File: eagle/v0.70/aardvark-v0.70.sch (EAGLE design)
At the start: 22 parts, among them IC1 REG1117, X1 MINI-USB-32005-201

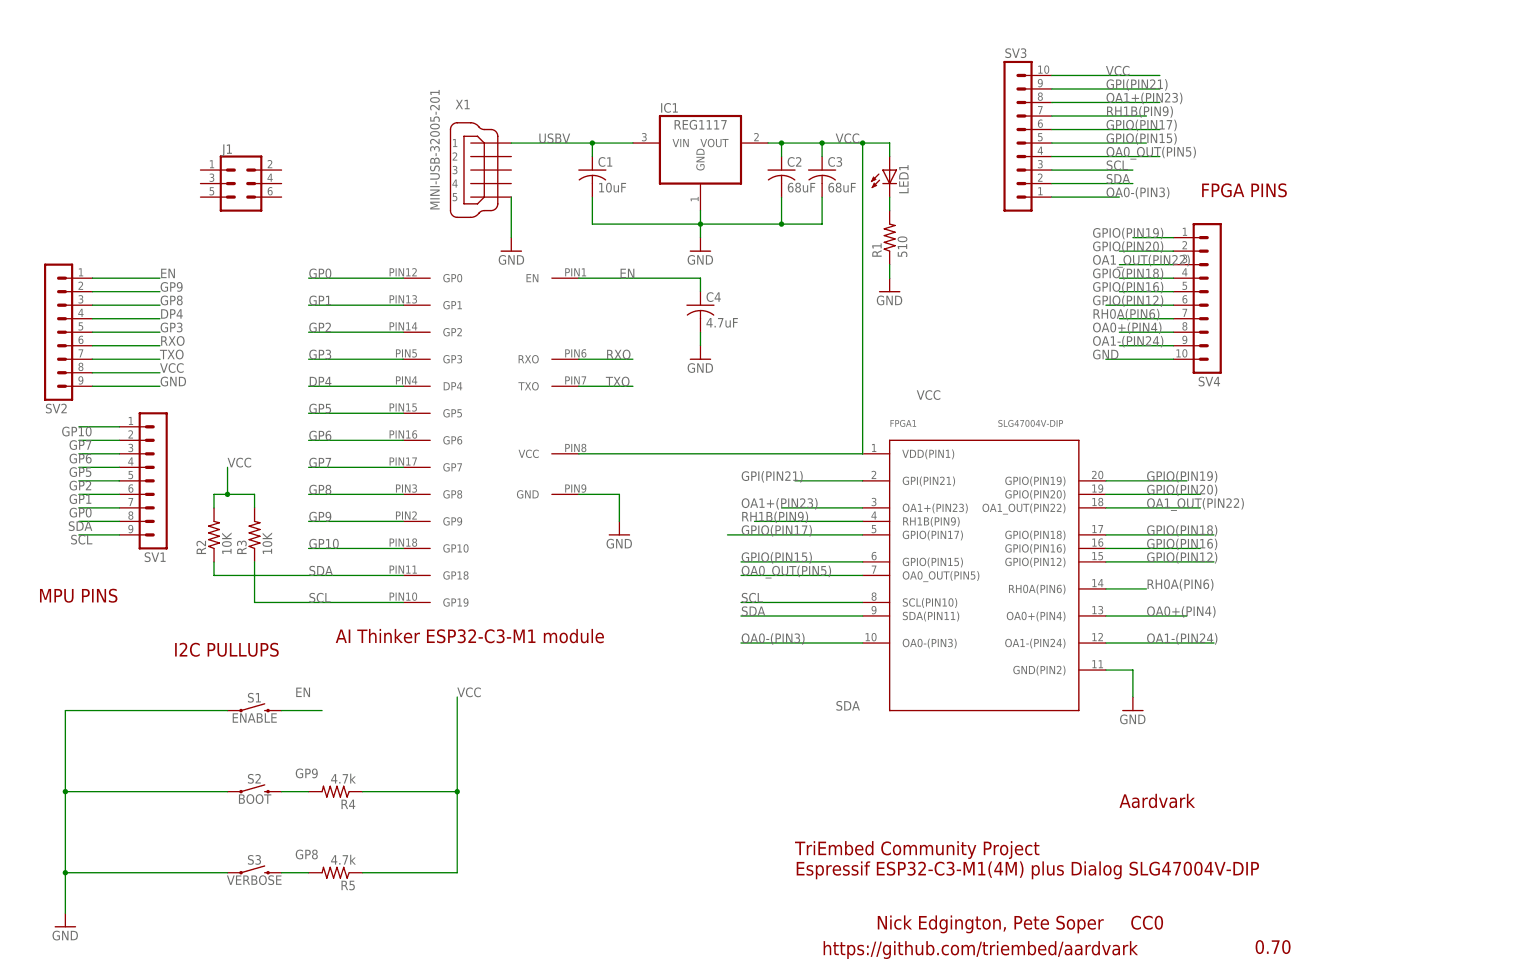
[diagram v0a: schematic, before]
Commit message: schematic update
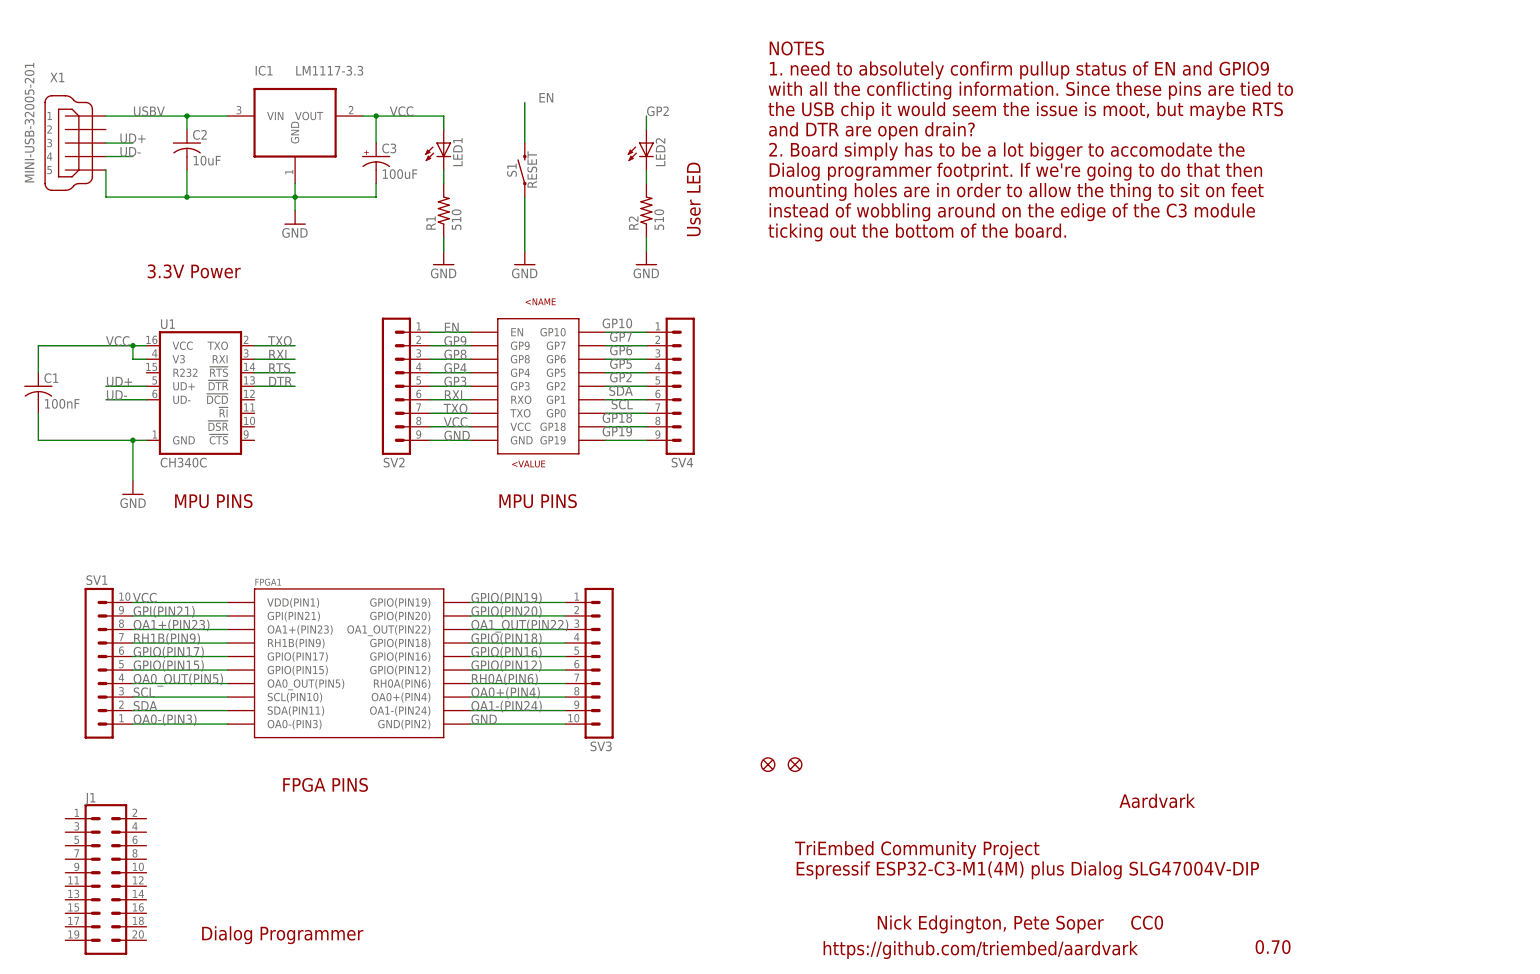
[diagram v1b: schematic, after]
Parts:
- removed C4: 4.7uF, rcl:C-USC0805
- removed R3: 10K, rcl:R-US_R0805
- removed R4, R5: 4.7k, rcl:R-US_R0805
- removed S2: BOOT, apexprotofactory:MOMENTARY-SWITCH-SPST-SMD-6.0X3.5MM
- removed S3: VERBOSE, apexprotofactory:MOMENTARY-SWITCH-SPST-SMD-6.0X3.5MM
- removed U$2: UNTITLED_ESP32C3, aardvark-v0.01:UNTITLED_ESP32C3
- added FD1, FD2: FIDUCIAL1X2, apexprotofactory:FIDUCIAL1X2
- added LED2: (no value), adafruit:LEDCHIP-LED0805
- added MOD1: (no value), aithinker-C3-M1:ESPRESSIF_ESP32C3
- added U1: CH340C, SparkFun-IC-Comms:CH340C
- C1: value 10uF -> 100nF
- C2: value 68uF -> 10uF; device rcl:C-USC1206 -> rcl:C-USC0805
- C3: value 68uF -> 100uF; device rcl:C-USC1206 -> SparkFun-Capacitors:100UF-POLAR-25V-20%(ELEC)
- FPGA1: value SLG47004V-DIP -> (none); device 22020117-1206PM-SLG47004V-DIP:SLG7004V_DIP -> SLG47004V-DIP:SLG7004V_DIP
- IC1: value REG1117 -> LM1117-3.3
- J1: device SparkFun-Connectors:CONN_03X2NO_SILK -> SparkFun-Connectors:CONN_10X2
- R2: value 10K -> 510
- S1: value ENABLE -> RESET; device apexprotofactory:MOMENTARY-SWITCH-SPST-SMD-6.0X3.5MM -> SparkFun-Switches:MOMENTARY-SWITCH-SPST-SMD-6.0X3.5MM
- SV1: device con-lstb:MA09-1 -> con-lstb:MA10-1
- SV4: device con-lstb:MA10-1 -> con-lstb:MA09-1
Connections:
- removed net DP4: SV2.4, U$2.DP4
- removed net GP0: SV1.7, U$2.GP0
- removed net GP1: SV1.6, U$2.GP1
- removed net RXO: SV2.6, U$2.RXO
- new net DTR: U1.!DTR
- new net GP18: MOD1.GP18, SV4.8
- new net GP19: MOD1.GP19, SV4.9
- new net GP4: MOD1.GP4, SV2.4
- new net N$1: LED2.C, R2.2
- new net RTS: U1.!RTS
- new net RXI: MOD1.RXO, SV2.6, U1.RXI
- new net UD+: U1.UD+, X1.3
- new net UD-: U1.UD-, X1.4
- net EN: now also MOD1.EN; no longer C4.1, U$2.EN
- net GND: now also C3.-, MOD1.GND, R2.1, SV3.10, U1.GND; no longer C3.2, C4.2, S2.1, S3.1, SV4.10, U$2.GND
- net GP10: now also MOD1.GP10, SV4.1; no longer SV1.1, U$2.GP10
- net GP2: now also LED2.A, MOD1.GP2, SV4.5; no longer SV1.5, U$2.GP2
- net GP3: now also MOD1.GP3; no longer U$2.GP3
- net GP5: now also MOD1.GP5, SV4.4; no longer SV1.4, U$2.GP5
- net GP6: now also MOD1.GP6, SV4.3; no longer SV1.3, U$2.GP6
- net GP7: now also MOD1.GP7, SV4.2; no longer SV1.2, U$2.GP7
- net GP8: now also MOD1.GP8; no longer R5.2, S3.2, U$2.GP8
- net GP9: now also MOD1.GP9; no longer R4.2, S2.2, U$2.GP9
- net GPI(PIN21): now also SV1.9; no longer SV3.9
- net GPIO(PIN12): now also SV3.6; no longer SV4.6
- net GPIO(PIN15): now also SV1.5; no longer SV3.5
- net GPIO(PIN16): now also SV3.5; no longer SV4.5
- net GPIO(PIN17): now also SV1.6; no longer SV3.6
- net GPIO(PIN18): now also SV3.4; no longer SV4.4
- net GPIO(PIN19): now also SV3.1; no longer SV4.1
- net GPIO(PIN20): now also SV3.2; no longer SV4.2
- net OA0+(PIN4): now also SV3.8; no longer SV4.8
- net OA0-(PIN3): now also SV1.1; no longer SV3.1
- net OA0_OUT(PIN5): now also SV1.4; no longer SV3.4
- net OA1+(PIN23): now also SV1.8; no longer SV3.8
- net OA1-(PIN24): now also SV3.9; no longer SV4.9
- net OA1_OUT(PIN22): now also SV3.3; no longer SV4.3
- net RH0A(PIN6): now also SV3.7; no longer SV4.7
- net RH1B(PIN9): now also SV1.7; no longer SV3.7
- net SCL: now also MOD1.GP0, SV1.3, SV4.7; no longer R3.1, SV1.9, SV3.3, U$2.GP19
- net SDA: now also MOD1.GP1, SV1.2, SV4.6; no longer R2.1, SV1.8, SV3.2, U$2.GP18
- net TXO: now also MOD1.TXO, U1.TXO; no longer U$2.TXO
- net USBV: now also C2.1; no longer C1.1
- net VCC: now also C1.1, C3.+, MOD1.VCC, SV1.10, U1.V3, U1.VCC; no longer C2.1, C3.1, R2.2, R3.2, R4.1, R5.1, SV3.10, U$2.VCC
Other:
- note added: "3.3V Power"
- note added: "Dialog Programmer"
- note added: "NOTES 1. need to absolutely confirm pullup status of EN and GPIO9 with all the conflicting information. Since these pins are tied to the USB chip it would seem the issue is moot, but maybe RTS and DTR are open drain? 2. Board simply has to be a lot bigger to accomodate the Dialog programmer footprint. If we're going to do that then mounting holes are in order to allow the thing to sit on feet ins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"
- note added: "User LED"
- note removed: "AI Thinker ESP32-C3-M1 module"
- note removed: "I2C PULLUPS"
- moved on the sheet: C1, C2, IC1, LED1, R1, R2, S1, SV2, SV3, X1

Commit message: Fix C3 module footprint, shift pin outside SLG footprint, update notes
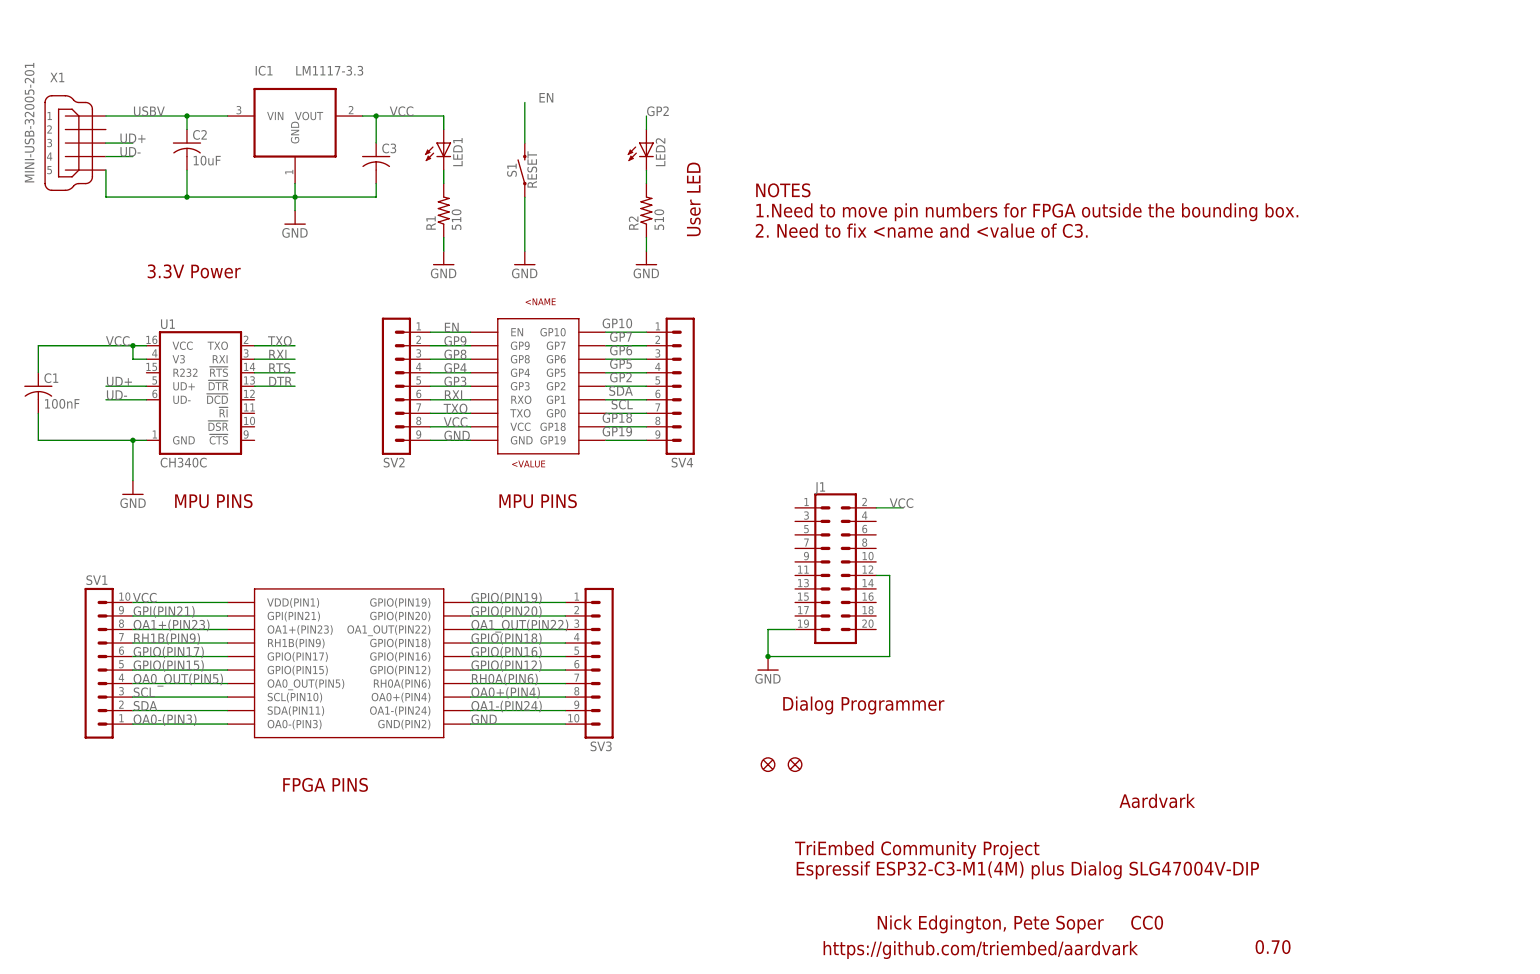
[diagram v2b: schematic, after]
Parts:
- C3: value 100uF -> (none); device SparkFun-Capacitors:100UF-POLAR-25V-20%(ELEC) -> rcl:C-USC1206
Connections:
- net GND: now also C3.2, J1.12, J1.19; no longer C3.-
- net VCC: now also C3.1, J1.2; no longer C3.+
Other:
- note added: "NOTES 1.Need to move pin numbers for FPGA outside the bounding box. 2. Need to fix <name and <value of C3."
- note removed: "NOTES 1. need to absolutely confirm pullup status of EN and GPIO9 with all the conflicting information. Since these pins are tied to the USB chip it would seem the issue is moot, but maybe RTS and DTR are open drain? 2. Board simply has to be a lot bigger to accomodate the Dialog programmer footprint. If we're going to do that then mounting holes are in order to allow the thing to sit on feet ins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"
- moved on the sheet: J1

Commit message: added right angle header site for outboard I2C programming
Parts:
- added SV5: (no value), con-lstb:MA04-1
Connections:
- net GND: now also SV5.1
- net SCL: now also SV5.3
- net SDA: now also SV5.4
- net VCC: now also SV5.2
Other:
- note added: "I2C for outboard programming"
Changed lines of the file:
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@@
 <part name="FPGA1" library="SLG47004V-DIP" deviceset="SLG7004V_DIP" device=""/>
 <part name="MOD1" library="aithinker-C3-M1" deviceset="ESPRESSIF_ESP32C3" device=""/>
+<part name="SV5" library="con-lstb" library_urn="urn:adsk.eagle:library:162" deviceset="MA04-1" device="" package3d_urn="urn:adsk.eagle:package:8337/1"/>
 </parts>
 <sheets>
@@
 2. Need to fix &lt;name and &lt;value of C3.
 </text>
+<text x="190.5" y="63.5" size="2.54" layer="94">I2C for outboard programming</text>
 </plain>
 <instances>
@@
 <instance part="FPGA1" gate="FPGA1" x="68.58" y="60.96" smashed="yes"/>
 <instance part="MOD1" gate="G$1" x="104.14" y="111.76" smashed="yes"/>
+<instance part="SV5" gate="1" x="195.58" y="78.74" smashed="yes">
+<attribute name="VALUE" x="194.31" y="68.58" size="1.778" layer="96"/>
+<attribute name="NAME" x="194.31" y="84.582" size="1.778" layer="95"/>
+</instance>
 </instances>
 <busses>
@@
 <wire x1="167.64" y1="88.9" x2="172.72" y2="88.9" width="0.1524" layer="91"/>
 <label x="170.18" y="88.9" size="1.778" layer="95"/>
+</segment>
+<segment>
+<pinref part="SV5" gate="1" pin="2"/>
+<wire x1="203.2" y1="76.2" x2="208.28" y2="76.2" width="0.1524" layer="91"/>
+<label x="203.2" y="76.2" size="1.778" layer="95"/>
 </segment>
 </net>
@@
 <junction x="147.32" y="60.96"/>
 </segment>
+<segment>
+<pinref part="SV5" gate="1" pin="1"/>
+<wire x1="203.2" y1="73.66" x2="208.28" y2="73.66" width="0.1524" layer="91"/>
+<label x="203.2" y="73.66" size="1.778" layer="95"/>
+</segment>
 </net>
 <net name="SCL" class="0">
@@
 <pinref part="MOD1" gate="G$1" pin="GP0"/>
 </segment>
+<segment>
+<pinref part="SV5" gate="1" pin="3"/>
+<wire x1="203.2" y1="78.74" x2="208.28" y2="78.74" width="0.1524" layer="91"/>
+<label x="203.2" y="78.74" size="1.778" layer="95"/>
+</segment>
 </net>
 <net name="SDA" class="0">
@@
 <pinref part="MOD1" gate="G$1" pin="GP1"/>
 </segment>
-</net>
+<segment>
+<pinref part="SV5" gate="1" pin="4"/>
+<wire x1="203.2" y1="81.28" x2="208.28" y2="81.28" width="0.1524" layer="91"/>
+<label x="203.2" y="81.28" size="1.778" layer="95"/>
+</segment>
+</net>

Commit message: 0.70 release candidate
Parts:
- removed X1: MINI-USB-32005-201, con-cypressindustries:MINI-USB-32005-201
- added DIALOG-PGM: (no value), SparkFun-Connectors:CONN_10X2
- added LOGO1: OSHW-LOGOMINI, SparkFun-Aesthetics:OSHW-LOGOMINI
- C1: value 100nF -> 10uF
- C2: value 10uF -> 100uF; device rcl:C-USC0805 -> SparkFun-Capacitors:47UF-POLAR-PANASONIC_D-50V-20%
- C3: value (none) -> 4.7uF; device rcl:C-USC1206 -> rcl:C-USC0805
- FPGA1: value (none) -> SLG47004V-DIP; device SLG47004V-DIP:SLG7004V_DIP -> SLG47004V-DIP:SLG47004V_DIP
- J1: value (none) -> USB_MINI-B_SMT; device SparkFun-Connectors:CONN_10X2 -> SparkFun-Connectors:USB_MINI-B_SMT
- LED1, LED2: device adafruit:LEDCHIP-LED0805 -> led:LEDCHIP-LED0805
- MOD1: value (none) -> ESP32-C3-M1; device aithinker-C3-M1:ESPRESSIF_ESP32C3 -> aithinker-C3-M1:AITHINKER-C3-M1
- SV2: device con-lstb:MA09-1 -> con-lstb:MA04-1
- SV3: device con-lstb:MA10-1 -> con-lstb:MA09-1
- SV4: device con-lstb:MA09-1 -> con-lstb:MA10-1
- SV5: device con-lstb:MA04-1 -> con-lstb:MA09-1
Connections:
- removed net DTR: U1.!DTR
- removed net RTS: U1.!RTS
- removed net USBV: C2.1, IC1.VIN, X1.1
- new net VBUS: C1.1, IC1.VIN, J1.VBUS
- net EN: now also C3.1, SV3.1, U1.!RTS; no longer SV2.1
- net GND: now also C2.-, DIALOG-PGM.12, DIALOG-PGM.19, J1.GND, SV2.1, SV3.9, SV4.10; no longer C2.2, J1.12, J1.19, SV2.9, SV3.10, SV5.1, X1.5
- net GP10: now also SV5.1; no longer SV4.1
- net GP18: now also SV5.8; no longer SV4.8
- net GP19: now also SV5.9; no longer SV4.9
- net GP2: now also SV5.5; no longer SV4.5
- net GP3: now also SV3.5; no longer SV2.5
- net GP4: now also SV3.4; no longer SV2.4
- net GP5: now also SV5.4; no longer SV4.4
- net GP6: now also SV5.3; no longer SV4.3
- net GP7: now also SV5.2; no longer SV4.2
- net GP8: now also SV3.3; no longer SV2.3
- net GP9: now also SV3.2, U1.!DTR; no longer SV2.2
- net GPIO(PIN12): now also SV4.6; no longer SV3.6
- net GPIO(PIN16): now also SV4.5; no longer SV3.5
- net GPIO(PIN18): now also SV4.4; no longer SV3.4
- net GPIO(PIN19): now also SV4.1; no longer SV3.1
- net GPIO(PIN20): now also SV4.2; no longer SV3.2
- net OA0+(PIN4): now also SV4.8; no longer SV3.8
- net OA1-(PIN24): now also SV4.9; no longer SV3.9
- net OA1_OUT(PIN22): now also SV4.3; no longer SV3.3
- net RH0A(PIN6): now also SV4.7; no longer SV3.7
- net RXI: now also SV3.6; no longer SV2.6
- net SCL: now also DIALOG-PGM.8, SV2.3, SV5.7; no longer SV4.7, SV5.3
- net SDA: now also DIALOG-PGM.9, SV2.4, SV5.6; no longer SV4.6, SV5.4
- net TXO: now also SV3.7; no longer SV2.7
- net UD+: now also J1.D+; no longer X1.3
- net UD-: now also J1.D-; no longer X1.4
- net VCC: now also C2.+, DIALOG-PGM.2, SV2.2, SV3.8; no longer C1.1, C3.1, J1.2, SV2.8, SV5.2
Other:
- note added: "Nick Edgington, Pete Soper CC BY-SA 2.0"
- note added: "USB Interface"
- note removed: "NOTES 1.Need to move pin numbers for FPGA outside the bounding box. 2. Need to fix <name and <value of C3."
- note removed: "Nick Edgington, Pete Soper CC0"
- moved on the sheet: C1, C3

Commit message: aardvark v0.70 as shipped to OSH Park
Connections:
- net SCL: now also SV2.4; no longer SV2.3
- net SDA: now also SV2.3; no longer SV2.4
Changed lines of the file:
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@@
-</segment>
-<segment>
-<pinref part="SV2" gate="1" pin="3"/>
-<wire x1="58.42" y1="22.86" x2="63.5" y2="22.86" width="0.1524" layer="91"/>
-<label x="58.42" y="22.86" size="1.778" layer="95"/>
 </segment>
 <segment>
@@
 <wire x1="167.64" y1="81.28" x2="172.72" y2="81.28" width="0.1524" layer="91"/>
 <label x="170.18" y="81.28" size="1.778" layer="95"/>
+</segment>
+<segment>
+<pinref part="SV2" gate="1" pin="4"/>
+<wire x1="58.42" y1="25.4" x2="63.5" y2="25.4" width="0.1524" layer="91"/>
+<label x="58.42" y="25.4" size="1.778" layer="95"/>
 </segment>
 </net>
@@
 </segment>
 <segment>
-<pinref part="SV2" gate="1" pin="4"/>
-<wire x1="58.42" y1="25.4" x2="63.5" y2="25.4" width="0.1524" layer="91"/>
-<label x="58.42" y="25.4" size="1.778" layer="95"/>
-</segment>
-<segment>
 <pinref part="DIALOG-PGM" gate="G$1" pin="9"/>
 <wire x1="152.4" y1="78.74" x2="144.78" y2="78.74" width="0.1524" layer="91"/>
 <label x="144.78" y="78.74" size="1.778" layer="95"/>
 </segment>
+<segment>
+<pinref part="SV2" gate="1" pin="3"/>
+<wire x1="58.42" y1="22.86" x2="63.5" y2="22.86" width="0.1524" layer="91"/>
+<label x="58.42" y="22.86" size="1.778" layer="95"/>
+</segment>
 </net>
